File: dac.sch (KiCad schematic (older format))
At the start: 46 parts, among them U15 OPA4172, U4 OPA4172, U8 DAC8568C

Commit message: added package field
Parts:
- C12, C13, C16, C17, C26, C28, C29, C3, C34, C35, C38, C39, C4, C48, C49, R20, R21, R22, R23, R26, R27, R32, R33, R39, R40, R41, R42, R45, R46, R49, R50, R51, R52, R54, R55, R57, R58, R60, R61, R62, R63: Package (none) -> 0603
- C27, C30: Package (none) -> 0805
- U15, U4: Package (none) -> SOIC-14
- U8: Package (none) -> TSSOP-16

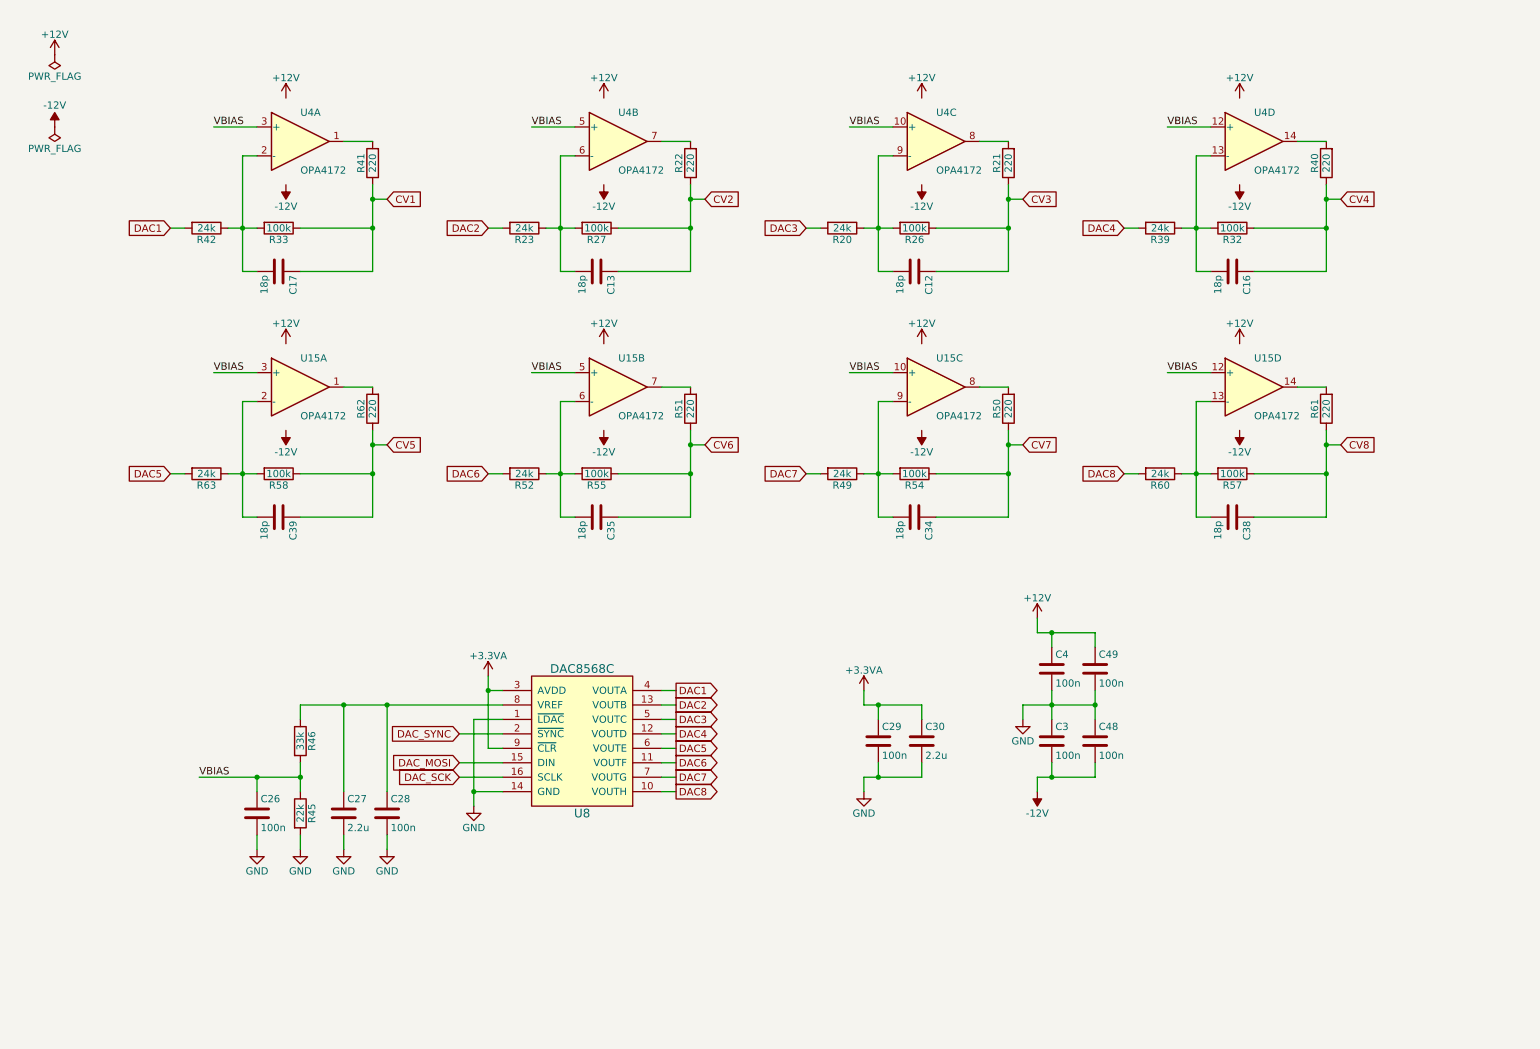
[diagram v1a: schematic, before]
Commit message: renumbered components
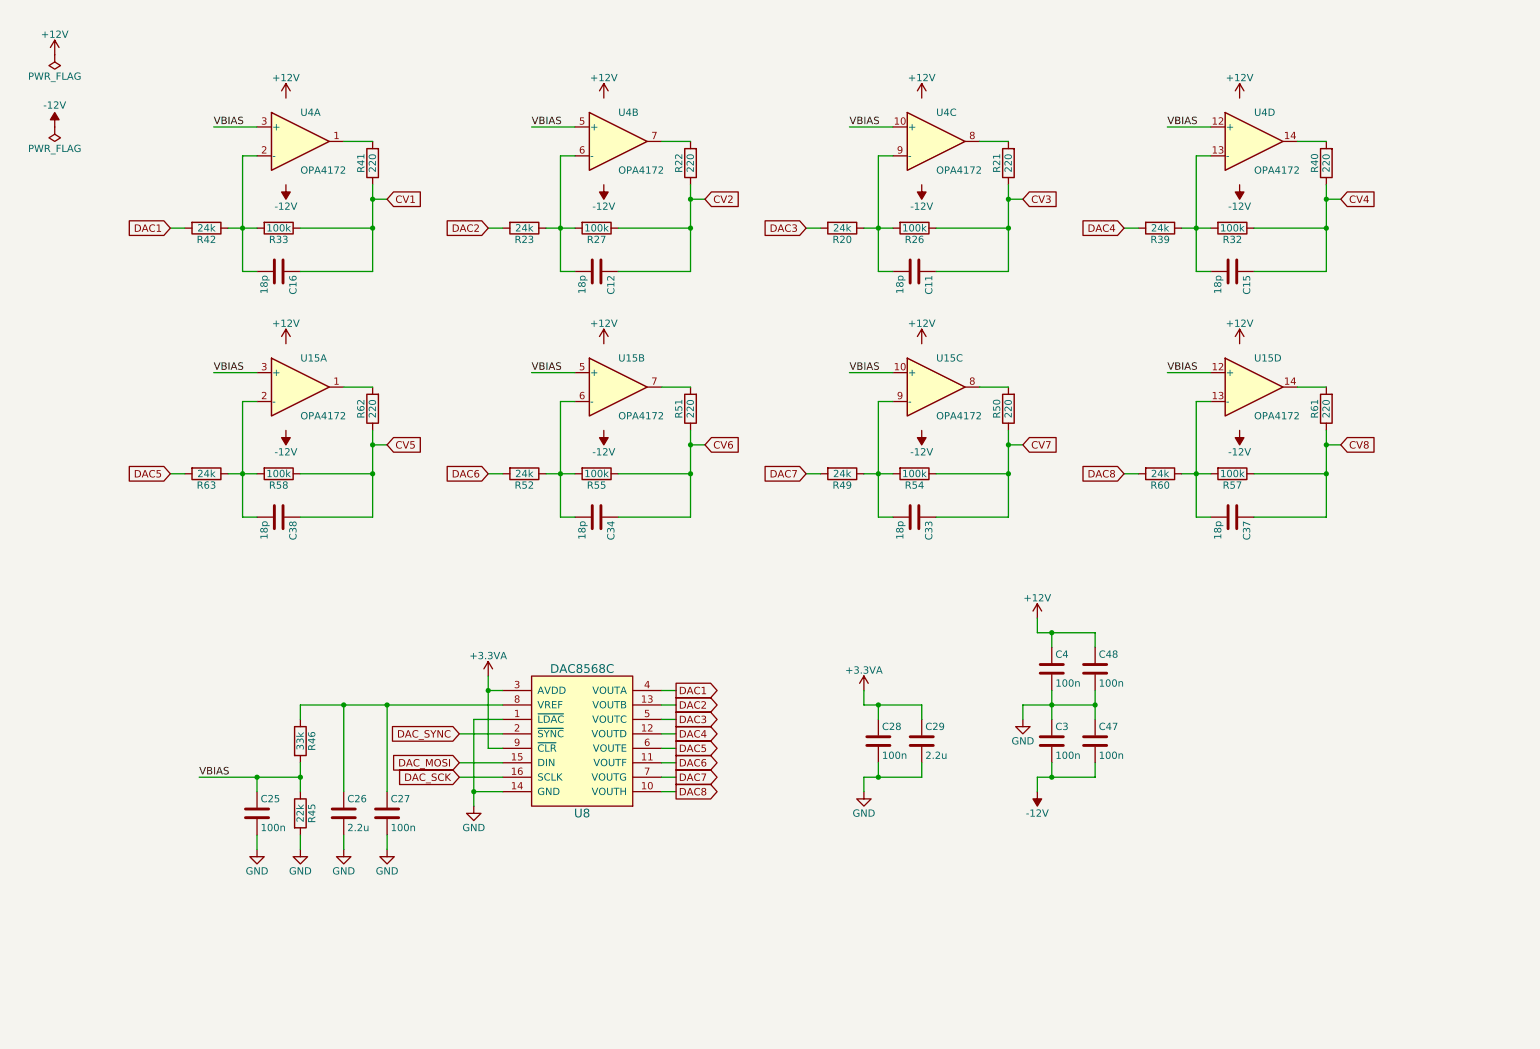
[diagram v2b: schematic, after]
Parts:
- renumbered C12 to C11, C13 to C12, C16 to C15, C17 to C16, C26 to C25, C27 to C26, C28 to C27, C29 to C28, C30 to C29, C34 to C33, C35 to C34, C38 to C37, C39 to C38, C48 to C47, C49 to C48
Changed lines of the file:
@@
 $EndComp
 $Comp
-L C C17
+L C C16
 U 1 1 59E36CC8
 P 2450 2400
-F 0 "C17" H 2475 2500 50  0000 L CNN
+F 0 "C16" H 2475 2500 50  0000 L CNN
 F 1 "18p" H 2475 2300 50  0000 L CNN
 F 2 "w_capacitor:C_0603" H 2488 2250 50  0001 C CNN
@@
 $EndComp
 $Comp
-L C C13
+L C C12
 U 1 1 59E399A8
 P 4650 2400
-F 0 "C13" H 4675 2500 50  0000 L CNN
+F 0 "C12" H 4675 2500 50  0000 L CNN
 F 1 "18p" H 4675 2300 50  0000 L CNN
 F 2 "w_capacitor:C_0603" H 4688 2250 50  0001 C CNN
@@
 $EndComp
 $Comp
-L C C12
+L C C11
 U 1 1 59E39C8D
 P 6850 2400
-F 0 "C12" H 6875 2500 50  0000 L CNN
+F 0 "C11" H 6875 2500 50  0000 L CNN
 F 1 "18p" H 6875 2300 50  0000 L CNN
 F 2 "w_capacitor:C_0603" H 6888 2250 50  0001 C CNN
@@
 $EndComp
 $Comp
-L C C16
+L C C15
 U 1 1 59E39CD6
 P 9050 2400
-F 0 "C16" H 9075 2500 50  0000 L CNN
+F 0 "C15" H 9075 2500 50  0000 L CNN
 F 1 "18p" H 9075 2300 50  0000 L CNN
 F 2 "w_capacitor:C_0603" H 9088 2250 50  0001 C CNN
@@
 $EndComp
 $Comp
-L C C39
+L C C38
 U 1 1 59E3B29C
 P 2450 4100
-F 0 "C39" H 2475 4200 50  0000 L CNN
+F 0 "C38" H 2475 4200 50  0000 L CNN
 F 1 "18p" H 2475 4000 50  0000 L CNN
 F 2 "w_capacitor:C_0603" H 2488 3950 50  0001 C CNN
@@
 $EndComp
 $Comp
-L C C35
+L C C34
 U 1 1 59E3B2E1
 P 4650 4100
-F 0 "C35" H 4675 4200 50  0000 L CNN
+F 0 "C34" H 4675 4200 50  0000 L CNN
 F 1 "18p" H 4675 4000 50  0000 L CNN
 F 2 "w_capacitor:C_0603" H 4688 3950 50  0001 C CNN
@@
 $EndComp
 $Comp
-L C C34
+L C C33
 U 1 1 59E3B326
 P 6850 4100
-F 0 "C34" H 6875 4200 50  0000 L CNN
+F 0 "C33" H 6875 4200 50  0000 L CNN
 F 1 "18p" H 6875 4000 50  0000 L CNN
 F 2 "w_capacitor:C_0603" H 6888 3950 50  0001 C CNN
@@
 $EndComp
 $Comp
-L C C38
+L C C37
 U 1 1 59E3B36B
 P 9050 4100
-F 0 "C38" H 9075 4200 50  0000 L CNN
+F 0 "C37" H 9075 4200 50  0000 L CNN
 F 1 "18p" H 9075 4000 50  0000 L CNN
 F 2 "w_capacitor:C_0603" H 9088 3950 50  0001 C CNN
@@
 $EndComp
 $Comp
-L C C49
+L C C48
 U 1 1 59E3BEA4
 P 8100 5150
-F 0 "C49" H 8125 5250 50  0000 L CNN
+F 0 "C48" H 8125 5250 50  0000 L CNN
 F 1 "100n" H 8125 5050 50  0000 L CNN
 F 2 "w_capacitor:C_0603" H 8138 5000 50  0001 C CNN
@@
 $EndComp
 $Comp
-L C C48
+L C C47
 U 1 1 59E3BFD0
 P 8100 5650
-F 0 "C48" H 8125 5750 50  0000 L CNN
+F 0 "C47" H 8125 5750 50  0000 L CNN
 F 1 "100n" H 8125 5550 50  0000 L CNN
 F 2 "w_capacitor:C_0603" H 8138 5500 50  0001 C CNN
@@
 $EndComp
 $Comp
-L C C29
+L C C28
 U 1 1 59E8511F
 P 6600 5650
-F 0 "C29" H 6625 5750 50  0000 L CNN
+F 0 "C28" H 6625 5750 50  0000 L CNN
 F 1 "100n" H 6625 5550 50  0000 L CNN
 F 2 "w_capacitor:C_0603" H 6638 5500 50  0001 C CNN
@@
 $EndComp
 $Comp
-L C C30
+L C C29
 U 1 1 59E8519C
 P 6900 5650
-F 0 "C30" H 6925 5750 50  0000 L CNN
+F 0 "C29" H 6925 5750 50  0000 L CNN
 F 1 "2.2u" H 6925 5550 50  0000 L CNN
 F 2 "w_capacitor:C_0805" H 6938 5500 50  0001 C CNN
@@
 $EndComp
 $Comp
-L C C28
+L C C27
 U 1 1 59E89082
 P 3200 6150
-F 0 "C28" H 3225 6250 50  0000 L CNN
+F 0 "C27" H 3225 6250 50  0000 L CNN
 F 1 "100n" H 3225 6050 50  0000 L CNN
 F 2 "w_capacitor:C_0603" H 3238 6000 50  0001 C CNN
@@
 $EndComp
 $Comp
-L C C27
+L C C26
 U 1 1 59E8908A
 P 2900 6150
-F 0 "C27" H 2925 6250 50  0000 L CNN
+F 0 "C26" H 2925 6250 50  0000 L CNN
 F 1 "2.2u" H 2925 6050 50  0000 L CNN
 F 2 "w_capacitor:C_0805" H 2938 6000 50  0001 C CNN
@@
 $EndComp
 $Comp
-L C C26
+L C C25
 U 1 1 59F01EC8
 P 2300 6150
-F 0 "C26" H 2325 6250 50  0000 L CNN
+F 0 "C25" H 2325 6250 50  0000 L CNN
 F 1 "100n" H 2325 6050 50  0000 L CNN
 F 2 "w_capacitor:C_0603" H 2338 6000 50  0001 C CNN

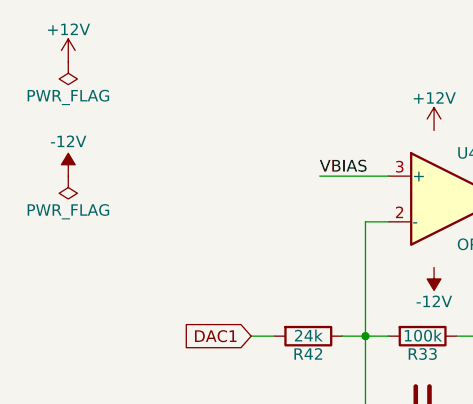
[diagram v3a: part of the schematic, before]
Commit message: cleanup schematics and updated to revision 0.3
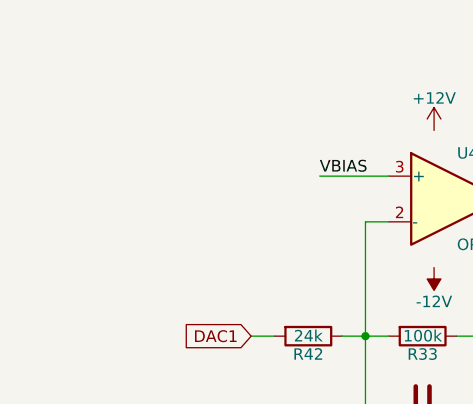
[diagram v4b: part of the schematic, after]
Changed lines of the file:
@@
 Sheet 8 8
 Title "per|former eurorack sequencer"
-Date ""
-Rev "0.2"
+Date "2018-08-26"
+Rev "0.3"
 Comp "westlicht"
 Comment1 "cc-by-sa"
@@
 $EndComp
 $Comp
-L GND #PWR0122
+L GND #PWR0125
 U 1 1 59DDC913
 P 3800 6100
-F 0 "#PWR0122" H 3800 5850 50  0001 C CNN
+F 0 "#PWR0125" H 3800 5850 50  0001 C CNN
 F 1 "GND" H 3800 5950 50  0000 C CNN
 F 2 "" H 3800 6100 50  0001 C CNN
@@
 $EndComp
 $Comp
-L +12V #PWR0123
+L +12V #PWR0126
 U 1 1 59E02DC5
 P 2500 1200
-F 0 "#PWR0123" H 2500 1050 50  0001 C CNN
+F 0 "#PWR0126" H 2500 1050 50  0001 C CNN
 F 1 "+12V" H 2500 1340 50  0000 C CNN
 F 2 "" H 2500 1200 50  0001 C CNN
@@
 $EndComp
 $Comp
-L +12V #PWR0124
+L +12V #PWR0127
 U 1 1 59E399A0
 P 4700 1200
-F 0 "#PWR0124" H 4700 1050 50  0001 C CNN
+F 0 "#PWR0127" H 4700 1050 50  0001 C CNN
 F 1 "+12V" H 4700 1340 50  0000 C CNN
 F 2 "" H 4700 1200 50  0001 C CNN
@@
 $EndComp
 $Comp
-L +12V #PWR0125
+L +12V #PWR0128
 U 1 1 59E39C85
 P 6900 1200
-F 0 "#PWR0125" H 6900 1050 50  0001 C CNN
+F 0 "#PWR0128" H 6900 1050 50  0001 C CNN
 F 1 "+12V" H 6900 1340 50  0000 C CNN
 F 2 "" H 6900 1200 50  0001 C CNN
@@
 $EndComp
 $Comp
-L +12V #PWR0126
+L +12V #PWR0129
 U 1 1 59E39CCE
 P 9100 1200
-F 0 "#PWR0126" H 9100 1050 50  0001 C CNN
+F 0 "#PWR0129" H 9100 1050 50  0001 C CNN
 F 1 "+12V" H 9100 1340 50  0000 C CNN
 F 2 "" H 9100 1200 50  0001 C CNN
@@
 $EndComp
 $Comp
-L +12V #PWR0127
+L +12V #PWR0130
 U 1 1 59E3B294
 P 2500 2900
-F 0 "#PWR0127" H 2500 2750 50  0001 C CNN
+F 0 "#PWR0130" H 2500 2750 50  0001 C CNN
 F 1 "+12V" H 2500 3040 50  0000 C CNN
 F 2 "" H 2500 2900 50  0001 C CNN
@@
 $EndComp
 $Comp
-L +12V #PWR0128
+L +12V #PWR0131
 U 1 1 59E3B2D9
 P 4700 2900
-F 0 "#PWR0128" H 4700 2750 50  0001 C CNN
+F 0 "#PWR0131" H 4700 2750 50  0001 C CNN
 F 1 "+12V" H 4700 3040 50  0000 C CNN
 F 2 "" H 4700 2900 50  0001 C CNN
@@
 $EndComp
 $Comp
-L +12V #PWR0129
+L +12V #PWR0132
 U 1 1 59E3B31E
 P 6900 2900
-F 0 "#PWR0129" H 6900 2750 50  0001 C CNN
+F 0 "#PWR0132" H 6900 2750 50  0001 C CNN
 F 1 "+12V" H 6900 3040 50  0000 C CNN
 F 2 "" H 6900 2900 50  0001 C CNN
@@
 $EndComp
 $Comp
-L +12V #PWR0130
+L +12V #PWR0133
 U 1 1 59E3B363
 P 9100 2900
-F 0 "#PWR0130" H 9100 2750 50  0001 C CNN
+F 0 "#PWR0133" H 9100 2750 50  0001 C CNN
 F 1 "+12V" H 9100 3040 50  0000 C CNN
 F 2 "" H 9100 2900 50  0001 C CNN
@@
 $EndComp
 $Comp
-L +12V #PWR0131
+L +12V #PWR0134
 U 1 1 59E3CBD7
 P 7700 4800
-F 0 "#PWR0131" H 7700 4650 50  0001 C CNN
+F 0 "#PWR0134" H 7700 4650 50  0001 C CNN
 F 1 "+12V" H 7700 4940 50  0000 C CNN
 F 2 "" H 7700 4800 50  0001 C CNN
@@
 $EndComp
 $Comp
-L GND #PWR0132
+L GND #PWR0135
 U 1 1 59E3CC72
 P 7600 5500
-F 0 "#PWR0132" H 7600 5250 50  0001 C CNN
+F 0 "#PWR0135" H 7600 5250 50  0001 C CNN
 F 1 "GND" H 7600 5350 50  0000 C CNN
 F 2 "" H 7600 5500 50  0001 C CNN
@@
 $EndComp
 $Comp
-L +3.3VA #PWR0133
+L +3.3VA #PWR0136
 U 1 1 59E85A18
 P 6500 5300
-F 0 "#PWR0133" H 6500 5150 50  0001 C CNN
+F 0 "#PWR0136" H 6500 5150 50  0001 C CNN
 F 1 "+3.3VA" H 6500 5440 50  0000 C CNN
 F 2 "" H 6500 5300 50  0001 C CNN
@@
 $EndComp
 $Comp
-L GND #PWR0134
+L GND #PWR0137
 U 1 1 59E85AB9
 P 6500 6000
-F 0 "#PWR0134" H 6500 5750 50  0001 C CNN
+F 0 "#PWR0137" H 6500 5750 50  0001 C CNN
 F 1 "GND" H 6500 5850 50  0000 C CNN
 F 2 "" H 6500 6000 50  0001 C CNN
@@
 $EndComp
 $Comp
-L GND #PWR0135
+L GND #PWR0138
 U 1 1 59E89BC5
 P 2900 6400
-F 0 "#PWR0135" H 2900 6150 50  0001 C CNN
+F 0 "#PWR0138" H 2900 6150 50  0001 C CNN
 F 1 "GND" H 2900 6250 50  0000 C CNN
 F 2 "" H 2900 6400 50  0001 C CNN
@@
 $EndComp
 $Comp
-L GND #PWR0136
+L GND #PWR0139
 U 1 1 59E89C6C
 P 3200 6400
-F 0 "#PWR0136" H 3200 6150 50  0001 C CNN
+F 0 "#PWR0139" H 3200 6150 50  0001 C CNN
 F 1 "GND" H 3200 6250 50  0000 C CNN
 F 2 "" H 3200 6400 50  0001 C CNN
@@
 $EndComp
 $Comp
-L +3.3VA #PWR0137
+L +3.3VA #PWR0140
 U 1 1 59EA8926
 P 3900 5200
-F 0 "#PWR0137" H 3900 5050 50  0001 C CNN
+F 0 "#PWR0140" H 3900 5050 50  0001 C CNN
 F 1 "+3.3VA" H 3900 5340 50  0000 C CNN
 F 2 "" H 3900 5200 50  0001 C CNN
@@
 $EndComp
 $Comp
-L GND #PWR0138
+L GND #PWR0141
 U 1 1 59F01739
 P 2600 6400
-F 0 "#PWR0138" H 2600 6150 50  0001 C CNN
+F 0 "#PWR0141" H 2600 6150 50  0001 C CNN
 F 1 "GND" H 2600 6250 50  0000 C CNN
 F 2 "" H 2600 6400 50  0001 C CNN
@@
 $EndComp
 $Comp
-L GND #PWR0139
+L GND #PWR0142
 U 1 1 59F021DB
 P 2300 6400
-F 0 "#PWR0139" H 2300 6150 50  0001 C CNN
+F 0 "#PWR0142" H 2300 6150 50  0001 C CNN
 F 1 "GND" H 2300 6250 50  0000 C CNN
 F 2 "" H 2300 6400 50  0001 C CNN
@@
 	1    0    0    -1
 $EndComp
-$Comp
-L +12V #PWR0140
-U 1 1 59F3FADC
-P 900 900
-F 0 "#PWR0140" H 900 750 50  0001 C CNN
-F 1 "+12V" H 900 1040 50  0000 C CNN
-F 2 "" H 900 900 50  0001 C CNN
-F 3 "" H 900 900 50  0001 C CNN
-	1    900  900
-	1    0    0    -1
-$EndComp
-$Comp
-L -12V #PWR706
-U 1 1 59F3FE98
-P 900 1400
-F 0 "#PWR706" H 900 1500 50  0001 C CNN
-F 1 "-12V" H 900 1550 50  0000 C CNN
-F 2 "" H 900 1400 50  0001 C CNN
-F 3 "" H 900 1400 50  0001 C CNN
-	1    900  1400
-	1    0    0    -1
-$EndComp
-$Comp
-L PWR_FLAG #FLG0141
-U 1 1 59F40358
-P 900 900
-F 0 "#FLG0141" H 900 975 50  0001 C CNN
-F 1 "PWR_FLAG" H 900 1050 50  0000 C CNN
-F 2 "" H 900 900 50  0001 C CNN
-F 3 "" H 900 900 50  0001 C CNN
-	1    900  900
-	-1   0    0    1
-$EndComp
-$Comp
-L PWR_FLAG #FLG0142
-U 1 1 59F40408
-P 900 1400
-F 0 "#FLG0142" H 900 1475 50  0001 C CNN
-F 1 "PWR_FLAG" H 900 1550 50  0000 C CNN
-F 2 "" H 900 1400 50  0001 C CNN
-F 3 "" H 900 1400 50  0001 C CNN
-	1    900  1400
-	-1   0    0    1
-$EndComp
 Text GLabel 5200 5300 2    51   Output ~ 0

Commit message: cleaned up schematics
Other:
- note added: "CV OUTPUT BUFFERS"
- note added: "DIGITAL TO ANALOG CONVERTER"
- note added: "Inverting opamp configuration, Input range [0V,3.3V], Output range [5.17V,-5.25V]"
- moved on the sheet: C11, C12, C15, C16, C25, C26, C27, C28, C29, C3, C33, C34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
